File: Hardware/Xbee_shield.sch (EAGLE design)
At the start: 39 parts, among them Q1 MOSFET-NCHANNELSMD, Q2 MOSFET-NCHANNELSMD, U1 ARDUINO_SHIELD, U2 XBEE-1B3, U4 V_REG_LDOSMD

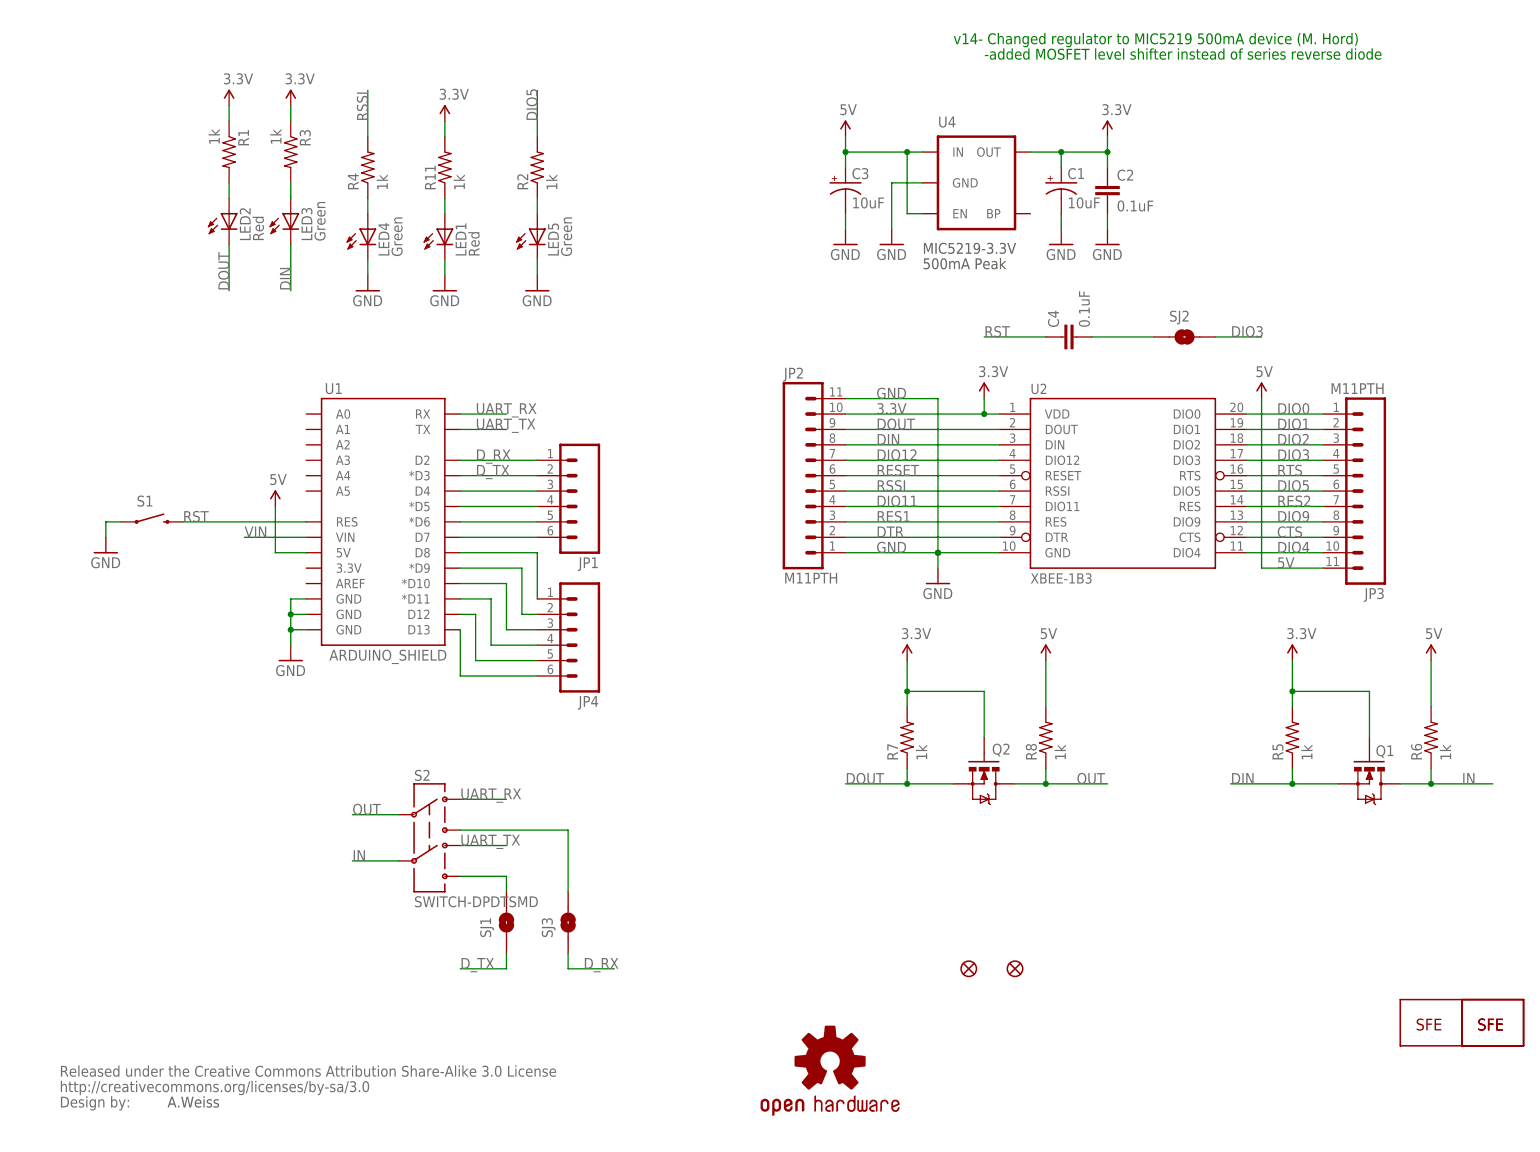
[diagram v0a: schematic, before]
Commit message: Updates to res/caps/r3 sheild, trace re routes
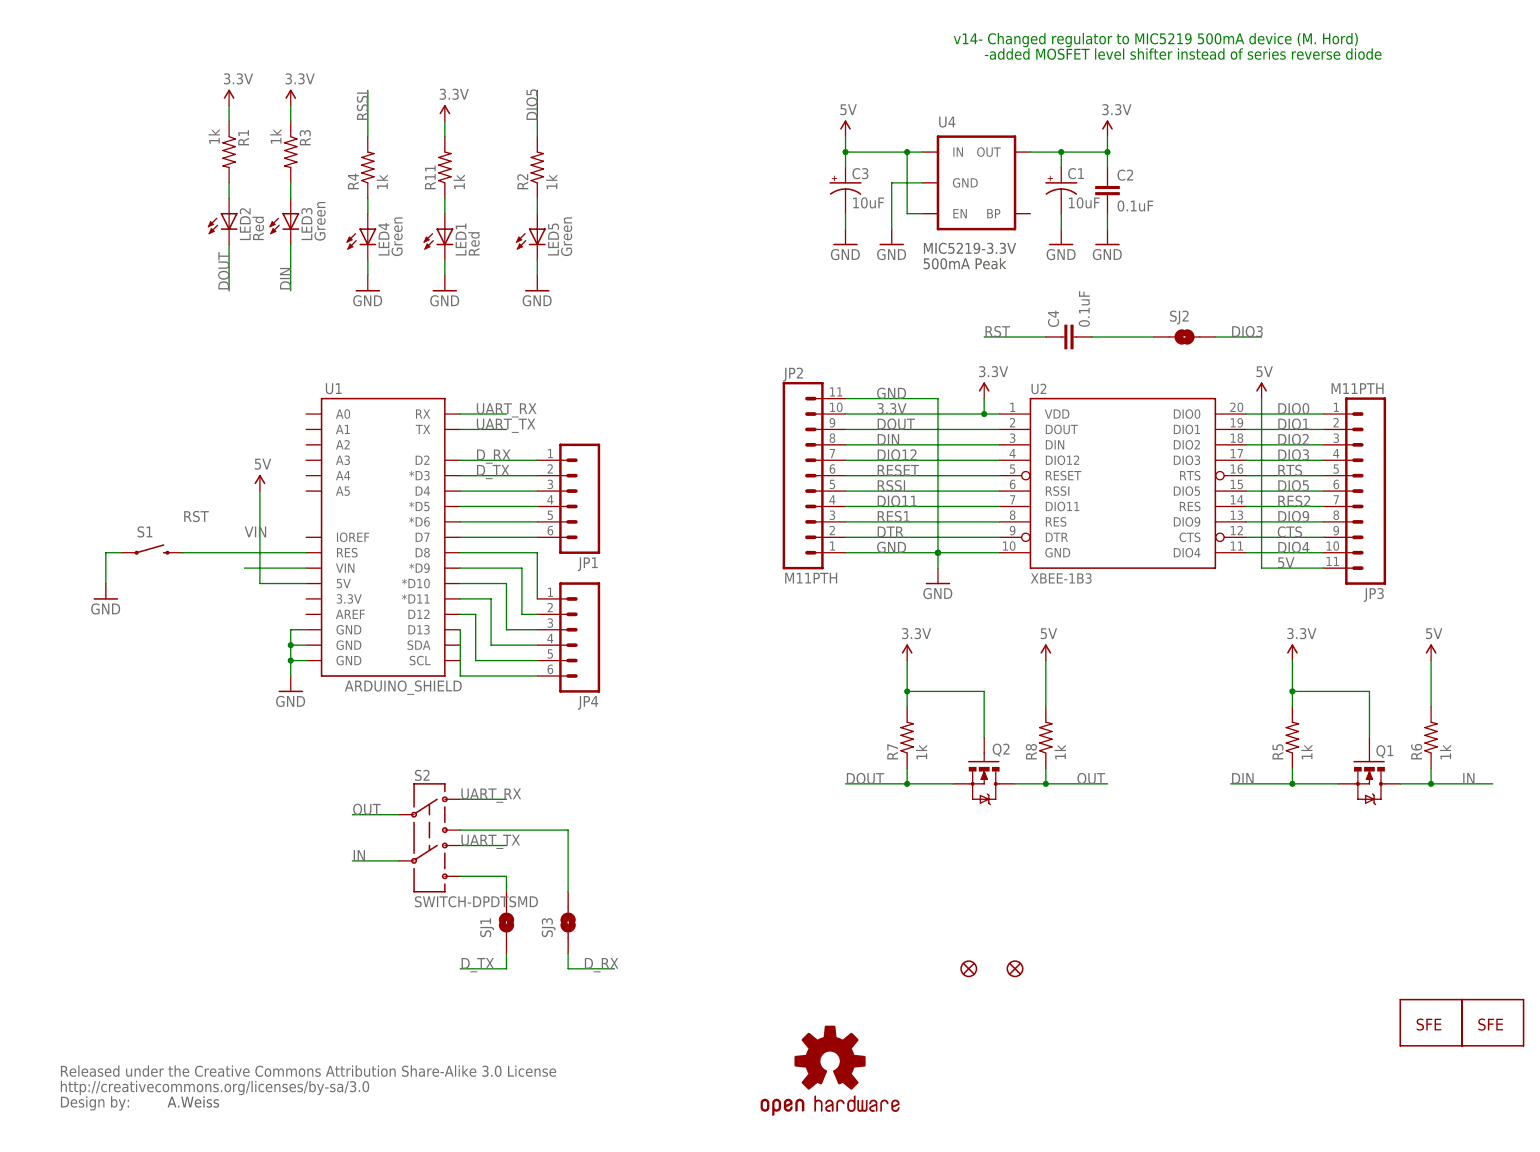
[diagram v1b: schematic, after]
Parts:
- removed U$4: LOGO-SFENEW, SparkFun:LOGO-SFENEW
- C2, C4: device SparkFun:CAP0402-CAP -> SparkFun-Capacitors:0.1UF-25V(+80/-20%)(0603)
- R1, R11, R2, R3, R4, R5, R6, R7, R8: device SparkFun:RESISTOR0402-RES -> SparkFun-Resistors:1KOHM1/10W1%(0603)
- U$8: value OSHW-LOGOS -> OSHW-LOGOL; device SparkFun-Aesthetics:OSHW-LOGOS -> SparkFun-Aesthetics:OSHW-LOGOL
- U1: device SparkFun:ARDUINO_SHIELDLABEL -> SparkFun-Boards:ARDUINO_R3_SHIELD
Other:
- moved on the sheet: S1
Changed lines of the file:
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@@
 <?xml version="1.0" encoding="utf-8"?>
 <!DOCTYPE eagle SYSTEM "eagle.dtd">
-<eagle version="6.0">
+<eagle version="6.4">
 <drawing>
 <settings>
@@
 <layer number="144" name="Drill_legend" color="7" fill="1" visible="yes" active="yes"/>
 <layer number="151" name="HeatSink" color="7" fill="1" visible="yes" active="yes"/>
+<layer number="199" name="Contour" color="7" fill="1" visible="yes" active="yes"/>
 <layer number="200" name="200bmp" color="1" fill="10" visible="no" active="no"/>
 <layer number="201" name="201bmp" color="2" fill="1" visible="no" active="no"/>
@@
 </classes>
 <parts>
-<part name="R11" library="SparkFun" deviceset="RESISTOR" device="0402-RES" value="1k"/>
+<part name="R11" library="SparkFun-Resistors" deviceset="1KOHM1/10W1%(0603)" device="" value="1k"/>
 <part name="LED1" library="SparkFun" deviceset="LED" device="0603" value="Red"/>
 <part name="GND28" library="SparkFun" deviceset="GND" device=""/>
 <part name="LED2" library="SparkFun" deviceset="LED" device="0603" value="Red"/>
 <part name="LED3" library="SparkFun" deviceset="LED" device="0603" value="Green"/>
-<part name="R1" library="SparkFun" deviceset="RESISTOR" device="0402-RES" value="1k"/>
-<part name="R3" library="SparkFun" deviceset="RESISTOR" device="0402-RES" value="1k"/>
+<part name="R1" library="SparkFun-Resistors" deviceset="1KOHM1/10W1%(0603)" device="" value="1k"/>
+<part name="R3" library="SparkFun-Resistors" deviceset="1KOHM1/10W1%(0603)" device="" value="1k"/>
 <part name="U$1" library="SparkFun" deviceset="LOGO-SFE" device="SK"/>
-<part name="U$4" library="SparkFun" deviceset="LOGO-SFE" device="NEW"/>
 <part name="U2" library="SparkFun" deviceset="XBEE-1" device="B3"/>
 <part name="P+1" library="SparkFun" deviceset="3.3V" device=""/>
 <part name="GND2" library="SparkFun" deviceset="GND" device=""/>
 <part name="LED4" library="SparkFun" deviceset="LED" device="0603" value="Green"/>
-<part name="R4" library="SparkFun" deviceset="RESISTOR" device="0402-RES" value="1k"/>
+<part name="R4" library="SparkFun-Resistors" deviceset="1KOHM1/10W1%(0603)" device="" value="1k"/>
 <part name="GND4" library="SparkFun" deviceset="GND" device=""/>
 <part name="GND1" library="SparkFun" deviceset="GND" device=""/>
 <part name="C1" library="SparkFun" deviceset="CAP_POL" device="1206" value="10uF"/>
-<part name="C2" library="SparkFun" deviceset="CAP" device="0402-CAP" value="0.1uF"/>
+<part name="C2" library="SparkFun-Capacitors" deviceset="0.1UF-25V(+80/-20%)(0603)" device="" value="0.1uF"/>
 <part name="GND3" library="SparkFun" deviceset="GND" device=""/>
 <part name="GND5" library="SparkFun" deviceset="GND" device=""/>
@@
 <part name="P+4" library="SparkFun" deviceset="3.3V" device=""/>
 <part name="FRAME1" library="SparkFun" deviceset="FRAME-LETTER" device=""/>
-<part name="U1" library="SparkFun" deviceset="ARDUINO_SHIELD" device="LABEL" value="ARDUINO_SHIELD"/>
+<part name="U1" library="SparkFun-Boards" deviceset="ARDUINO_R3_SHIELD" device="" value="ARDUINO_SHIELD"/>
 <part name="U$2" library="SparkFun" deviceset="5V" device=""/>
 <part name="U$3" library="SparkFun" deviceset="5V" device=""/>
@@
 <part name="GND8" library="SparkFun" deviceset="GND" device=""/>
 <part name="SJ2" library="SparkFun" deviceset="SOLDERJUMPER" device="TRACE"/>
-<part name="C4" library="SparkFun" deviceset="CAP" device="0402-CAP" value="0.1uF"/>
+<part name="C4" library="SparkFun-Capacitors" deviceset="0.1UF-25V(+80/-20%)(0603)" device="" value="0.1uF"/>
 <part name="LED5" library="SparkFun" deviceset="LED" device="0603" value="Green"/>
-<part name="R2" library="SparkFun" deviceset="RESISTOR" device="0402-RES" value="1k"/>
+<part name="R2" library="SparkFun-Resistors" deviceset="1KOHM1/10W1%(0603)" device="" value="1k"/>
 <part name="GND9" library="SparkFun" deviceset="GND" device=""/>
 <part name="S2" library="SparkFun" deviceset="SWITCH-DPDT" device="SMD"/>
@@
 <part name="U$5" library="SparkFun" deviceset="CREATIVE_COMMONS" device=""/>
 <part name="Q1" library="SparkFun-DiscreteSemi" deviceset="MOSFET-NCHANNEL" device="SMD"/>
-<part name="R5" library="SparkFun" deviceset="RESISTOR" device="0402-RES" value="1k"/>
-<part name="R6" library="SparkFun" deviceset="RESISTOR" device="0402-RES" value="1k"/>
+<part name="R5" library="SparkFun-Resistors" deviceset="1KOHM1/10W1%(0603)" device="" value="1k"/>
+<part name="R6" library="SparkFun-Resistors" deviceset="1KOHM1/10W1%(0603)" device="" value="1k"/>
 <part name="P+5" library="SparkFun" deviceset="3.3V" device=""/>
 <part name="U$6" library="SparkFun" deviceset="5V" device=""/>
 <part name="Q2" library="SparkFun-DiscreteSemi" deviceset="MOSFET-NCHANNEL" device="SMD"/>
-<part name="R7" library="SparkFun" deviceset="RESISTOR" device="0402-RES" value="1k"/>
-<part name="R8" library="SparkFun" deviceset="RESISTOR" device="0402-RES" value="1k"/>
+<part name="R7" library="SparkFun-Resistors" deviceset="1KOHM1/10W1%(0603)" device="" value="1k"/>
+<part name="R8" library="SparkFun-Resistors" deviceset="1KOHM1/10W1%(0603)" device="" value="1k"/>
 <part name="P+7" library="SparkFun" deviceset="3.3V" device=""/>
 <part name="U$7" library="SparkFun" deviceset="5V" device=""/>
-<part name="U$8" library="SparkFun-Aesthetics" deviceset="OSHW-LOGO" device="S"/>
+<part name="U$8" library="SparkFun-Aesthetics" deviceset="OSHW-LOGO" device="L" value="OSHW-LOGOL"/>
 <part name="U4" library="SparkFun-PowerIC" deviceset="V_REG_LDO" device="SMD"/>
 <part name="U$9" library="SparkFun" deviceset="5V" device=""/>
@@
 <instance part="R3" gate="G$1" x="45.72" y="162.56" rot="R270"/>
 <instance part="U$1" gate="G$1" x="241.3" y="17.78"/>
-<instance part="U$4" gate="G$1" x="241.3" y="17.78"/>
 <instance part="U2" gate="G$1" x="182.88" y="109.22"/>
 <instance part="P+1" gate="G$1" x="160.02" y="121.92"/>
@@
 <instance part="FRAME1" gate="G$2" x="147.32" y="0"/>
 <instance part="U1" gate="G$1" x="60.96" y="101.6"/>
-<instance part="U$2" gate="G$1" x="43.18" y="104.14"/>
+<instance part="U$2" gate="G$1" x="40.64" y="106.68"/>
 <instance part="U$3" gate="G$1" x="137.16" y="165.1"/>
 <instance part="P+6" gate="G$1" x="180.34" y="165.1"/>
-<instance part="GND7" gate="1" x="45.72" y="78.74"/>
-<instance part="S1" gate="G$1" x="22.86" y="101.6" smashed="yes">
-<attribute name="NAME" x="20.32" y="104.14" size="1.778" layer="95"/>
+<instance part="GND7" gate="1" x="45.72" y="73.66"/>
+<instance part="S1" gate="G$1" x="22.86" y="96.52" smashed="yes">
+<attribute name="NAME" x="20.32" y="99.06" size="1.778" layer="95"/>
 </instance>
-<instance part="GND8" gate="1" x="15.24" y="96.52"/>
+<instance part="GND8" gate="1" x="15.24" y="88.9"/>
 <instance part="SJ2" gate="1" x="193.04" y="132.08"/>
 <instance part="C4" gate="G$1" x="175.26" y="132.08" rot="R90"/>
@@
 </segment>
 <segment>
-<wire x1="48.26" y1="88.9" x2="45.72" y2="88.9" width="0.1524" layer="91"/>
-<wire x1="45.72" y1="88.9" x2="45.72" y2="86.36" width="0.1524" layer="91"/>
-<wire x1="45.72" y1="86.36" x2="45.72" y2="83.82" width="0.1524" layer="91"/>
+<wire x1="48.26" y1="83.82" x2="45.72" y2="83.82" width="0.1524" layer="91"/>
 <wire x1="45.72" y1="83.82" x2="45.72" y2="81.28" width="0.1524" layer="91"/>
-<wire x1="48.26" y1="86.36" x2="45.72" y2="86.36" width="0.1524" layer="91"/>
-<wire x1="48.26" y1="83.82" x2="45.72" y2="83.82" width="0.1524" layer="91"/>
-<junction x="45.72" y="86.36"/>
-<junction x="45.72" y="83.82"/>
+<wire x1="45.72" y1="81.28" x2="45.72" y2="78.74" width="0.1524" layer="91"/>
+<wire x1="45.72" y1="78.74" x2="45.72" y2="76.2" width="0.1524" layer="91"/>
+<wire x1="48.26" y1="81.28" x2="45.72" y2="81.28" width="0.1524" layer="91"/>
+<wire x1="48.26" y1="78.74" x2="45.72" y2="78.74" width="0.1524" layer="91"/>
+<junction x="45.72" y="81.28"/>
+<junction x="45.72" y="78.74"/>
 <pinref part="U1" gate="G$1" pin="GND@2"/>
 <pinref part="GND7" gate="1" pin="GND"/>
@@
 </segment>
 <segment>
-<wire x1="17.78" y1="101.6" x2="15.24" y2="101.6" width="0.1524" layer="91"/>
-<wire x1="15.24" y1="101.6" x2="15.24" y2="99.06" width="0.1524" layer="91"/>
+<wire x1="17.78" y1="96.52" x2="15.24" y2="96.52" width="0.1524" layer="91"/>
+<wire x1="15.24" y1="96.52" x2="15.24" y2="91.44" width="0.1524" layer="91"/>
 <pinref part="S1" gate="G$1" pin="1"/>
 <pinref part="GND8" gate="1" pin="GND"/>
@@
 </segment>
 <segment>
-<wire x1="48.26" y1="96.52" x2="43.18" y2="96.52" width="0.1524" layer="91"/>
-<wire x1="43.18" y1="96.52" x2="43.18" y2="104.14" width="0.1524" layer="91"/>
+<wire x1="48.26" y1="91.44" x2="40.64" y2="91.44" width="0.1524" layer="91"/>
+<wire x1="40.64" y1="91.44" x2="40.64" y2="106.68" width="0.1524" layer="91"/>
 <pinref part="U1" gate="G$1" pin="5V"/>
 <pinref part="U$2" gate="G$1" pin="5V"/>
@@
 <net name="RST" class="0">
 <segment>
-<wire x1="48.26" y1="101.6" x2="27.94" y2="101.6" width="0.1524" layer="91"/>
+<wire x1="48.26" y1="96.52" x2="27.94" y2="96.52" width="0.1524" layer="91"/>
 <label x="27.94" y="101.6" size="1.778" layer="95"/>
 <pinref part="U1" gate="G$1" pin="RES"/>
@@
 <segment>
 <pinref part="U1" gate="G$1" pin="VIN"/>
-<wire x1="48.26" y1="99.06" x2="38.1" y2="99.06" width="0.1524" layer="91"/>
+<wire x1="48.26" y1="93.98" x2="38.1" y2="93.98" width="0.1524" layer="91"/>
 <label x="38.1" y="99.06" size="1.778" layer="95"/>
 </segment>

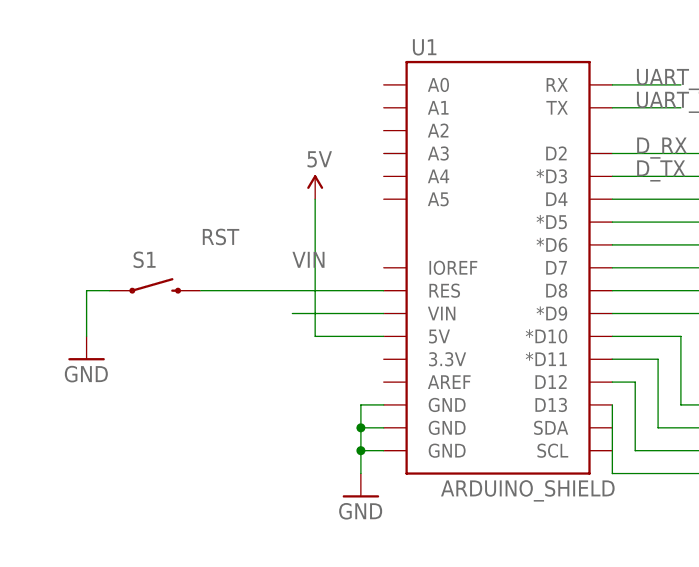
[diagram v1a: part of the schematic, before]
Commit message: Fixed LED's/Silk
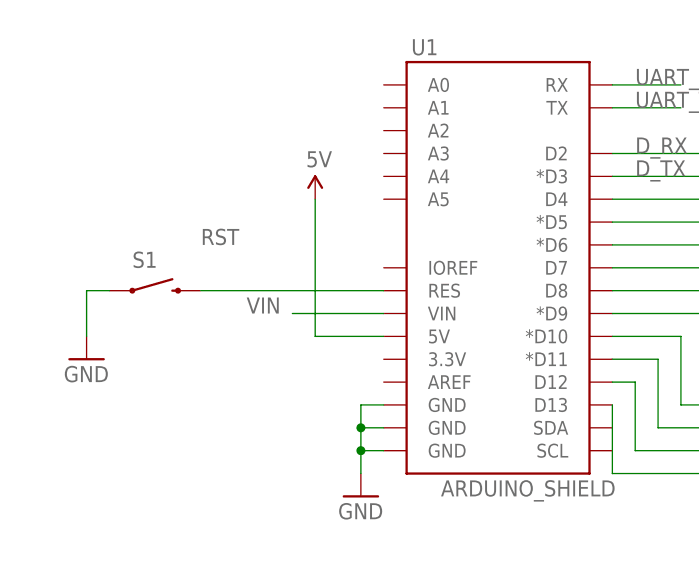
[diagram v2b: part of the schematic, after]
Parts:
- LED1, LED2: device SparkFun:LED0603 -> SparkFun-LED:LED-RED0603
- LED3, LED4, LED5: device SparkFun:LED0603 -> SparkFun-LED:LED-GREEN0603
- U$8: value OSHW-LOGOL -> OSHW-LOGOS; device SparkFun-Aesthetics:OSHW-LOGOL -> SparkFun-Aesthetics:OSHW-LOGOS
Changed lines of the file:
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@@
 <layer number="106" name="bPlate" color="7" fill="1" visible="yes" active="yes"/>
 <layer number="107" name="Crop" color="7" fill="1" visible="yes" active="yes"/>
+<layer number="108" name="tplace-old" color="10" fill="1" visible="yes" active="yes"/>
+<layer number="109" name="ref-old" color="11" fill="1" visible="yes" active="yes"/>
 <layer number="116" name="Patch_BOT" color="9" fill="4" visible="yes" active="yes"/>
 <layer number="121" name="_tsilk" color="7" fill="1" visible="yes" active="yes"/>
@@
 <parts>
 <part name="R11" library="SparkFun-Resistors" deviceset="1KOHM1/10W1%(0603)" device="" value="1k"/>
-<part name="LED1" library="SparkFun" deviceset="LED" device="0603" value="Red"/>
+<part name="LED1" library="SparkFun-LED" deviceset="LED-RED" device="0603" value="Red"/>
 <part name="GND28" library="SparkFun" deviceset="GND" device=""/>
-<part name="LED2" library="SparkFun" deviceset="LED" device="0603" value="Red"/>
-<part name="LED3" library="SparkFun" deviceset="LED" device="0603" value="Green"/>
+<part name="LED2" library="SparkFun-LED" deviceset="LED-RED" device="0603" value="Red"/>
+<part name="LED3" library="SparkFun-LED" deviceset="LED-GREEN" device="0603" value="Green"/>
 <part name="R1" library="SparkFun-Resistors" deviceset="1KOHM1/10W1%(0603)" device="" value="1k"/>
 <part name="R3" library="SparkFun-Resistors" deviceset="1KOHM1/10W1%(0603)" device="" value="1k"/>
@@
 <part name="P+1" library="SparkFun" deviceset="3.3V" device=""/>
 <part name="GND2" library="SparkFun" deviceset="GND" device=""/>
-<part name="LED4" library="SparkFun" deviceset="LED" device="0603" value="Green"/>
+<part name="LED4" library="SparkFun-LED" deviceset="LED-GREEN" device="0603" value="Green"/>
 <part name="R4" library="SparkFun-Resistors" deviceset="1KOHM1/10W1%(0603)" device="" value="1k"/>
 <part name="GND4" library="SparkFun" deviceset="GND" device=""/>
@@
 <part name="SJ2" library="SparkFun" deviceset="SOLDERJUMPER" device="TRACE"/>
 <part name="C4" library="SparkFun-Capacitors" deviceset="0.1UF-25V(+80/-20%)(0603)" device="" value="0.1uF"/>
-<part name="LED5" library="SparkFun" deviceset="LED" device="0603" value="Green"/>
+<part name="LED5" library="SparkFun-LED" deviceset="LED-GREEN" device="0603" value="Green"/>
 <part name="R2" library="SparkFun-Resistors" deviceset="1KOHM1/10W1%(0603)" device="" value="1k"/>
 <part name="GND9" library="SparkFun" deviceset="GND" device=""/>
@@
 <part name="P+7" library="SparkFun" deviceset="3.3V" device=""/>
 <part name="U$7" library="SparkFun" deviceset="5V" device=""/>
-<part name="U$8" library="SparkFun-Aesthetics" deviceset="OSHW-LOGO" device="L" value="OSHW-LOGOL"/>
+<part name="U$8" library="SparkFun-Aesthetics" deviceset="OSHW-LOGO" device="S" value="OSHW-LOGOS"/>
 <part name="U4" library="SparkFun-PowerIC" deviceset="V_REG_LDO" device="SMD"/>
 <part name="U$9" library="SparkFun" deviceset="5V" device=""/>
@@
 <pinref part="U1" gate="G$1" pin="VIN"/>
 <wire x1="48.26" y1="93.98" x2="38.1" y2="93.98" width="0.1524" layer="91"/>
-<label x="38.1" y="99.06" size="1.778" layer="95"/>
-</segment>
-</net>
+<label x="33.02" y="93.98" size="1.778" layer="95"/>
+</segment>
+</net>

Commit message: Sch work
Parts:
- removed U$1: LOGO-SFESK, SparkFun:LOGO-SFESK
- removed U$5: CREATIVE_COMMONS, SparkFun:CREATIVE_COMMONS
- added FRAME1: FRAME-LETTER, SparkFun-Aesthetics:FRAME-LETTER
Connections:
- net N$67: now also U1.SCL, U1.SDA
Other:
- note added: "Aaron Weiss"
- note added: "Revised by: Patrick Alberts"
- note added: "v15"
- note removed: "-added MOSFET level shifter instead of series reverse diode"
- note removed: "A.Weiss"
- note removed: "v14- Changed regulator to MIC5219 500mA device (M. Hord)"
- moved on the sheet: C1, C2, C3, C4, JP1, JP4, LED1, LED2, LED3, LED4, LED5, Q1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
